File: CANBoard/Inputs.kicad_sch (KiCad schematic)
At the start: 23 parts

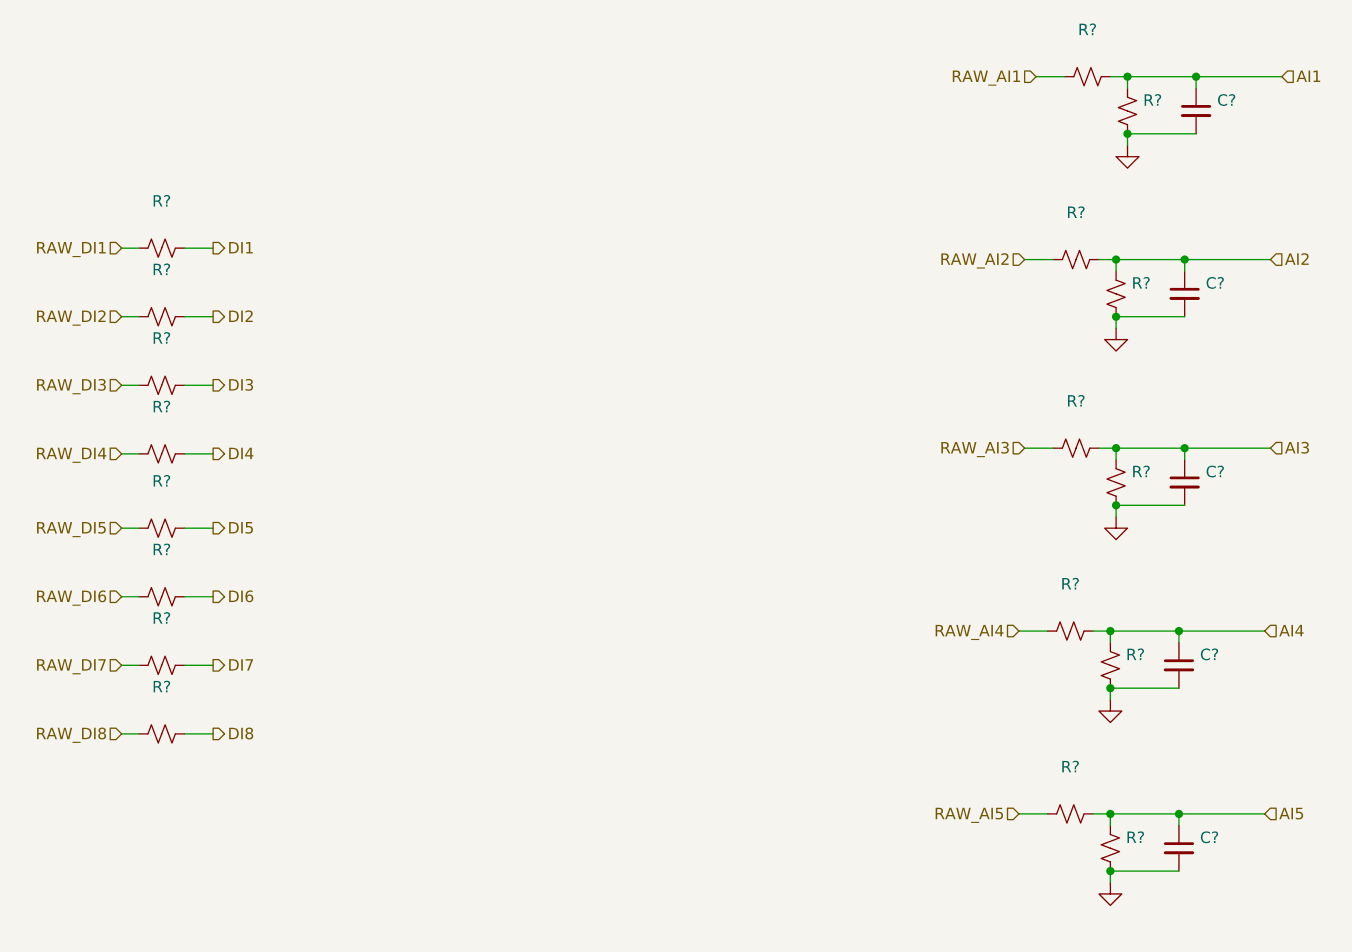
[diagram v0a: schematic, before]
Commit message: V2 updates
Removed FRAM, I2C and SWD pins. Added ID solder jumpers and Tag Connect
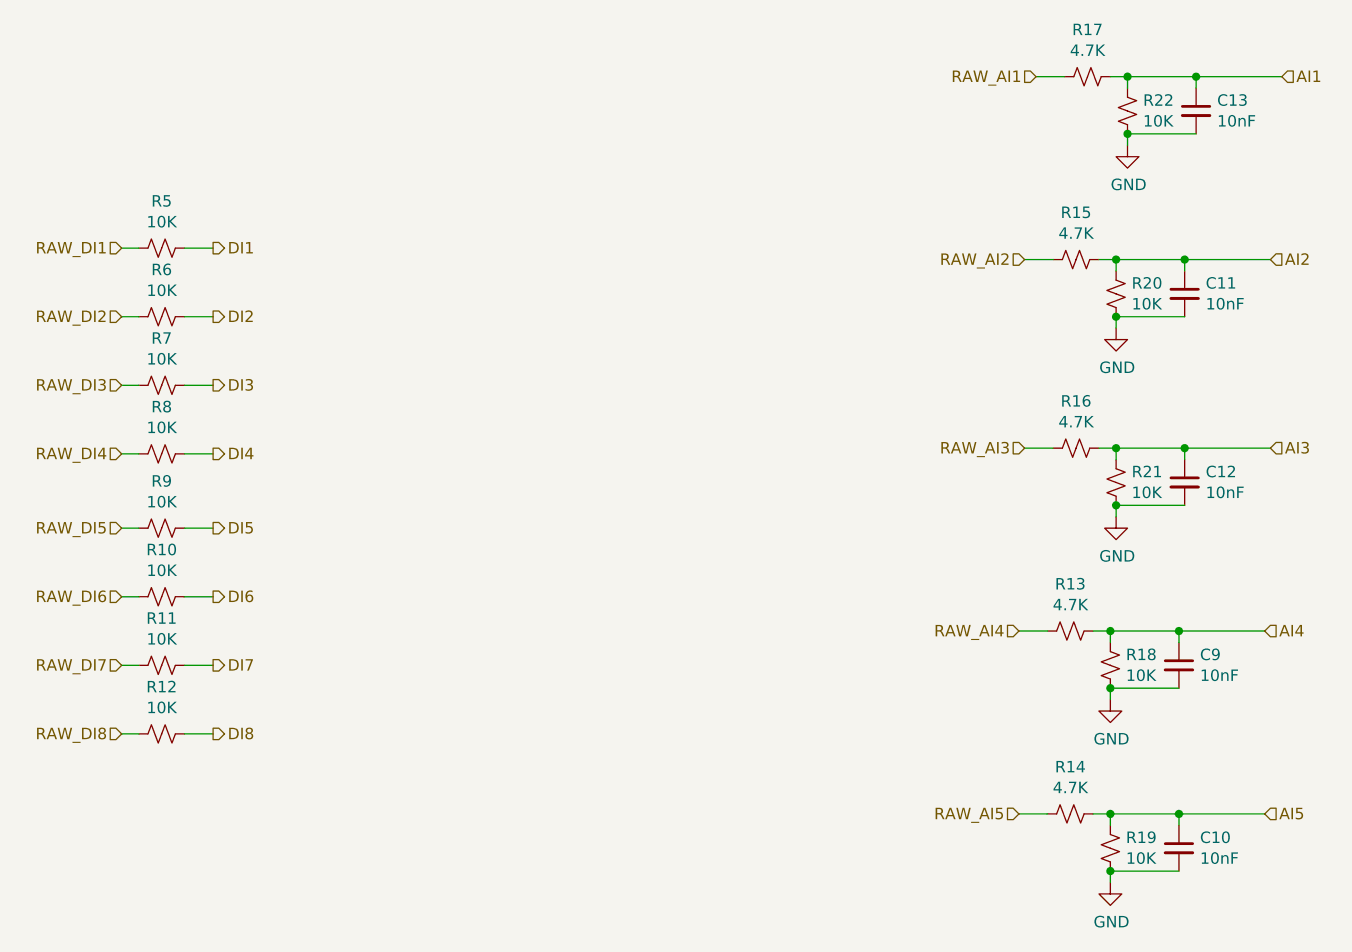
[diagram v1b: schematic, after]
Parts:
- C10, C11, C12, C13, C9: renamed from C?; value (none) -> 10nF; footprint (none) -> Capacitor_SMD:C_0805_2012Metric
- R10, R11, R12, R18, R19, R20, R21, R22, R5, R6, R7, R8, R9: renamed from R?; value (none) -> 10K; footprint (none) -> Resistor_SMD:R_0805_2012Metric
- R13, R14, R15, R16, R17: renamed from R?; value (none) -> 4.7K; footprint (none) -> Resistor_SMD:R_0805_2012Metric

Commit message: Updated outputs, added JLCPCB LCSC part nums
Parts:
- C10, C11, C12, C13, C9: LCSC (none) -> C1710
- R10, R11, R12, R18, R19, R20, R21, R22, R5, R6, R7, R8, R9: LCSC (none) -> C17414
- R13, R14, R15, R16, R17: LCSC (none) -> C17673
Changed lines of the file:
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@@
+      (effects (font (size 1.27 1.27)) hide)
+    )
+    (property "LCSC" "C17414" (at 66.675 102.87 0)
       (effects (font (size 1.27 1.27)) hide)
     )
@@
       (effects (font (size 1.27 1.27)) hide)
     )
+    (property "LCSC" "C17414" (at 66.675 95.25 0)
+      (effects (font (size 1.27 1.27)) hide)
+    )
     (pin "1")
     (pin "2")
@@
       (effects (font (size 1.27 1.27)) hide)
     )
+    (property "LCSC" "C17414" (at 66.675 87.63 0)
+      (effects (font (size 1.27 1.27)) hide)
+    )
     (pin "1")
     (pin "2")
@@
       (effects (font (size 1.27 1.27)) hide)
     )
+    (property "LCSC" "C17414" (at 66.675 80.01 0)
+      (effects (font (size 1.27 1.27)) hide)
+    )
     (pin "1")
     (pin "2")
@@
       (effects (font (size 1.27 1.27)) hide)
     )
+    (property "LCSC" "C17414" (at 66.675 71.755 0)
+      (effects (font (size 1.27 1.27)) hide)
+    )
     (pin "1")
     (pin "2")
@@
       (effects (font (size 1.27 1.27)) hide)
     )
+    (property "LCSC" "C17414" (at 66.675 64.135 0)
+      (effects (font (size 1.27 1.27)) hide)
+    )
     (pin "1")
     (pin "2")
@@
       (effects (font (size 1.27 1.27)) hide)
     )
+    (property "LCSC" "C17414" (at 66.675 56.515 0)
+      (effects (font (size 1.27 1.27)) hide)
+    )
     (pin "1")
     (pin "2")
@@
       (effects (font (size 1.27 1.27)) hide)
     )
+    (property "LCSC" "C17414" (at 66.675 48.895 0)
+      (effects (font (size 1.27 1.27)) hide)
+    )
     (pin "1")
     (pin "2")
@@
       (effects (font (size 1.27 1.27)) hide)
     )
+    (property "LCSC" "C17673" (at 169.545 29.845 0)
+      (effects (font (size 1.27 1.27)) hide)
+    )
     (pin "1")
     (pin "2")
@@
       (effects (font (size 1.27 1.27)) hide)
     )
+    (property "LCSC" "C17414" (at 173.99 33.655 0)
+      (effects (font (size 1.27 1.27)) hide)
+    )
     (pin "1")
     (pin "2")
@@
       (effects (font (size 1.27 1.27)) hide)
     )
+    (property "LCSC" "C1710" (at 181.61 33.655 0)
+      (effects (font (size 1.27 1.27)) hide)
+    )
     (pin "1")
     (pin "2")
@@
       (effects (font (size 1.27 1.27)) hide)
     )
+    (property "LCSC" "C17673" (at 168.275 50.165 0)
+      (effects (font (size 1.27 1.27)) hide)
+    )
     (pin "1")
     (pin "2")
@@
       (effects (font (size 1.27 1.27)) hide)
     )
+    (property "LCSC" "C17414" (at 172.72 53.975 0)
+      (effects (font (size 1.27 1.27)) hide)
+    )
     (pin "1")
     (pin "2")
@@
       (effects (font (size 1.27 1.27)) hide)
     )
+    (property "LCSC" "C1710" (at 180.34 53.975 0)
+      (effects (font (size 1.27 1.27)) hide)
+    )
     (pin "1")
     (pin "2")
@@
       (effects (font (size 1.27 1.27)) hide)
     )
+    (property "LCSC" "C17673" (at 168.275 71.12 0)
+      (effects (font (size 1.27 1.27)) hide)
+    )
     (pin "1")
     (pin "2")
@@
       (effects (font (size 1.27 1.27)) hide)
     )
+    (property "LCSC" "C17414" (at 172.72 74.93 0)
+      (effects (font (size 1.27 1.27)) hide)
+    )
     (pin "1")
     (pin "2")
@@
       (effects (font (size 1.27 1.27)) hide)
     )
+    (property "LCSC" "C1710" (at 180.34 74.93 0)
+      (effects (font (size 1.27 1.27)) hide)
+    )
     (pin "1")
     (pin "2")
@@
       (effects (font (size 1.27 1.27)) hide)
     )
+    (property "LCSC" "C17673" (at 167.64 91.44 0)
+      (effects (font (size 1.27 1.27)) hide)
+    )
     (pin "1")
     (pin "2")
@@
       (effects (font (size 1.27 1.27)) hide)
     )
+    (property "LCSC" "C17414" (at 172.085 95.25 0)
+      (effects (font (size 1.27 1.27)) hide)
+    )
     (pin "1")
     (pin "2")
@@
       (effects (font (size 1.27 1.27)) hide)
     )
+    (property "LCSC" "C1710" (at 179.705 95.25 0)
+      (effects (font (size 1.27 1.27)) hide)
+    )
     (pin "1")
     (pin "2")
@@
       (effects (font (size 1.27 1.27)) hide)
     )
+    (property "LCSC" "C17673" (at 167.64 111.76 0)
+      (effects (font (size 1.27 1.27)) hide)
+    )
     (pin "1")
     (pin "2")
@@
       (effects (font (size 1.27 1.27)) hide)
     )
+    (property "LCSC" "C17414" (at 172.085 115.57 0)
+      (effects (font (size 1.27 1.27)) hide)
+    )
     (pin "1")
     (pin "2")
@@
       (effects (font (size 1.27 1.27)) hide)
     )
+    (property "LCSC" "C1710" (at 179.705 115.57 0)
+      (effects (font (size 1.27 1.27)) hide)
+    )
